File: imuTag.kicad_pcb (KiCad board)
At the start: 4 copper layers, 41.3 x 40 mm, 47 parts, among them J1 Conn_02x05_Odd_Even, J2 Conn_01x04_Pin, J3 Conn_01x02_Pin, Q1 DMG2305UX-13, U1 E73-2G4M08S1C, U2 ME6211C30M5G-N, U3 GD25Q64ESIG, U4 LSM6DSV16XTR, U5 LIS2MDLTR, Y2 Crystal

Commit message: Update PCB layout
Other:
- board text added: "GPIO"
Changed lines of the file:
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@@
 			(at 0 -2.38 90)
 			(layer "F.SilkS")
+			(hide yes)
 			(effects
 				(font
@@
 			(at 0 -1.43 270)
 			(layer "F.SilkS")
+			(hide yes)
 			(effects
 				(font
@@
 	)
 	(gr_text "FLASH"
-		(at 174.2694 116.3066 0)
+		(at 175.8188 116.3574 0)
 		(layer "F.SilkS")
 		(effects
@@
 	)
 	(gr_text "Magn."
-		(at 165.9382 117.0432 0)
+		(at 165.5064 114.9096 90)
 		(layer "F.SilkS")
 		(effects
@@
 		)
 	)
+	(gr_text "GPIO"
+		(at 164.3634 118.7196 90)
+		(layer "F.SilkS")
+		(effects
+			(font
+				(size 1 1)
+				(thickness 0.1)
+			)
+			(justify left bottom)
+		)
+	)
 	(gr_text "BTN1"
 		(at 155.9052 107.3404 305)
@@
 	)
 	(segment
-		(start 162.0126 114.7656)
-		(end 162.797 114.7656)
-		(width 0.4)
-		(layer "F.Cu")
-		(net 1)
-	)
-	(segment
 		(start 185.200083 107.773099)
 		(end 185.110822 107.86236)
@@
 	)
 	(segment
+		(start 162.797 114.7656)
+		(end 162.0126 114.7656)
+		(width 0.4)
+		(layer "F.Cu")
+		(net 1)
+	)
+	(segment
 		(start 156.880857 110.830657)
 		(end 157.607 111.5568)
@@
 	)
 	(segment
-		(start 162.797 114.7656)
-		(end 163.3982 115.3668)
-		(width 0.4)
-		(layer "F.Cu")
-		(net 1)
-	)
-	(segment
 		(start 163.824354 93.442046)
 		(end 164.15 93.1164)
@@
 	)
 	(segment
+		(start 163.385825 114.490175)
+		(end 163.072425 114.490175)
+		(width 0.4)
+		(layer "F.Cu")
+		(net 1)
+	)
+	(segment
 		(start 174.953 103.6331)
 		(end 175.1827 103.6331)
@@
 	)
 	(segment
+		(start 163.072425 114.490175)
+		(end 162.797 114.7656)
+		(width 0.4)
+		(layer "F.Cu")
+		(net 1)
+	)
+	(segment
 		(start 165.344 99.2786)
 		(end 167.249 101.1836)
@@
 	)
 	(via
-		(at 163.3982 115.3668)
+		(at 163.385825 114.490175)
 		(size 0.6)
 		(drill 0.4)

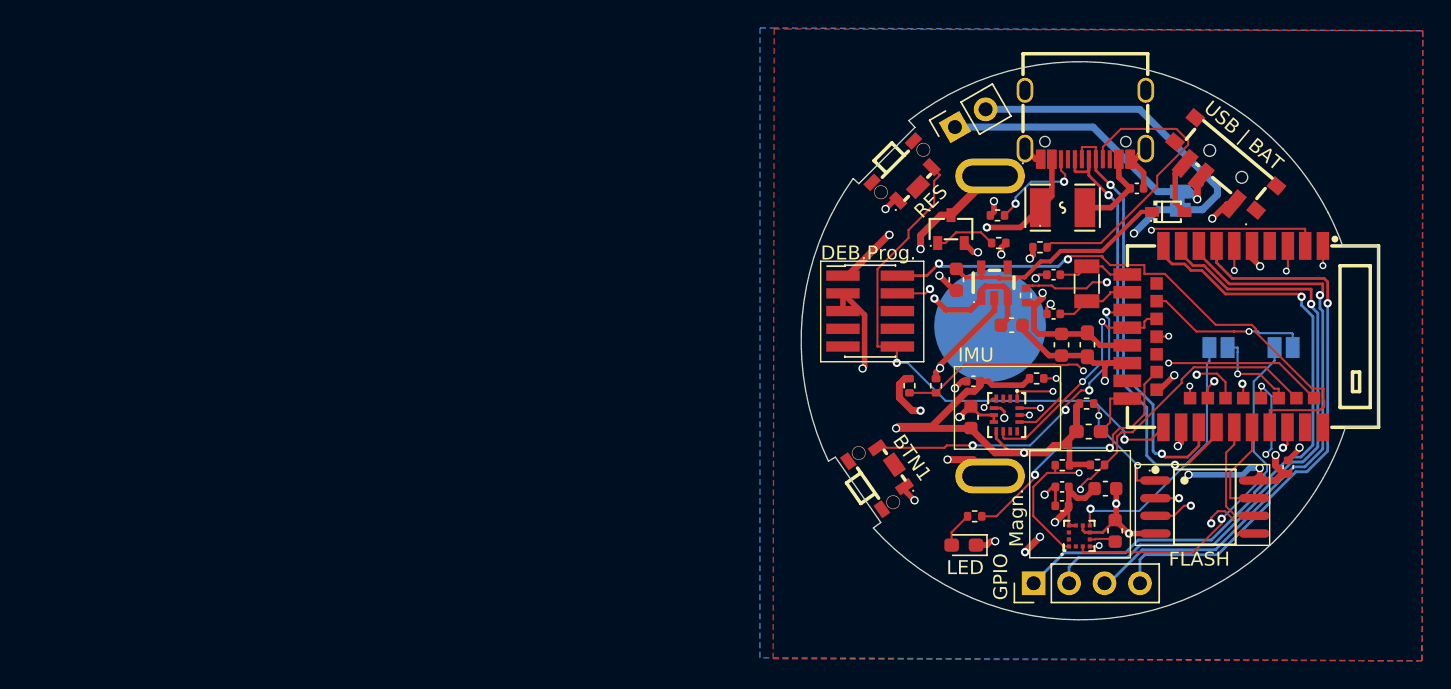
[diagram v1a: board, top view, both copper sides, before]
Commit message: feat: imuTag mini PCBA v1.0 – initial release
PCB layout, schematics (imuTag + sensors), custom EasyEDA symbol/footprint libraries with 3D models, design rules, and production outputs (BOM, placement, netlist).
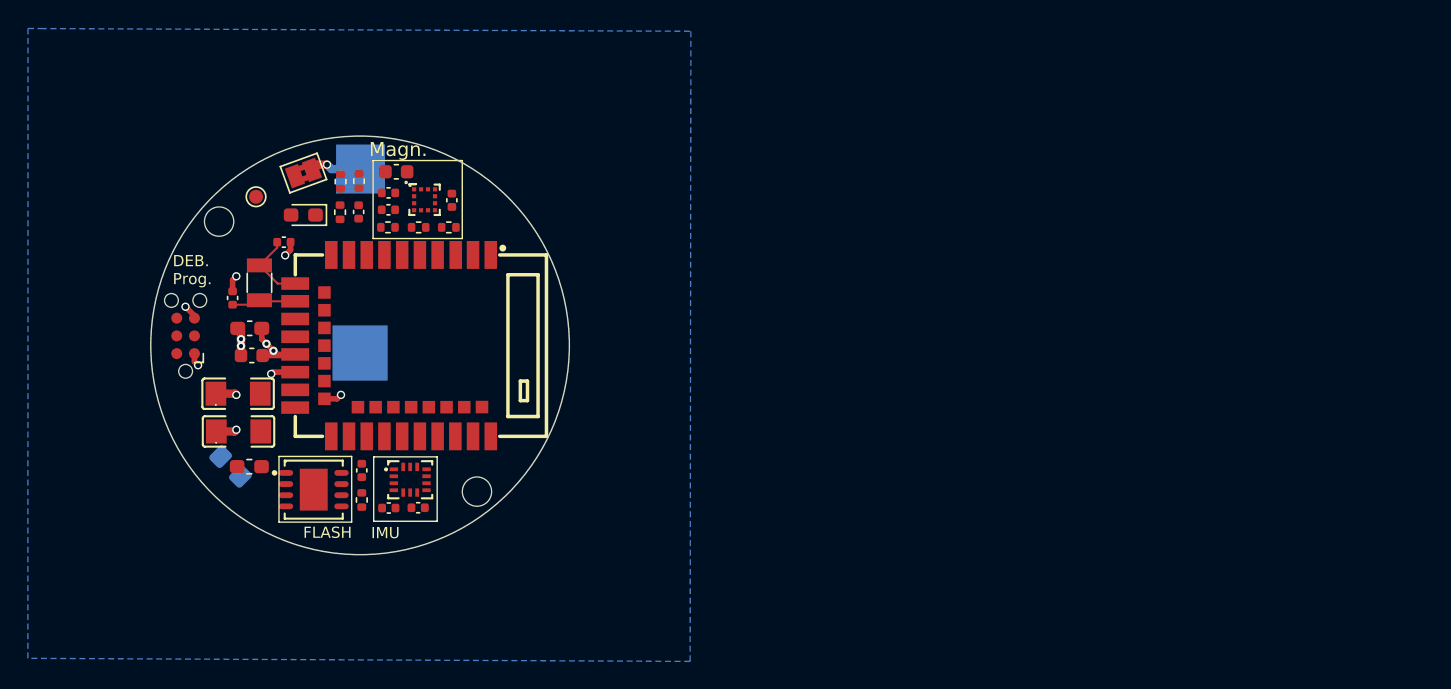
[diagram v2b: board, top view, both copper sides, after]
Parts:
- removed BAT1: BS-CR2032-8, EasyEDA:BAT-TH_MY-2032-22
- removed BTN1, RESET1: SW_Push, EasyEDA:SW-SMD_TS-1086EV-AR03526
- removed C3: 1u, Capacitor_SMD:C_0603_1608Metric
- removed D3: 1N5819WS, EasyEDA:SOD-323_L1.8-W1.3-LS2.5-RD
- removed F1: 1210L110/16WR, EasyEDA:F1210
- removed J2: Conn_01x04_Pin, Connector_PinHeader_2.54mm:PinHeader_1x04_P2.54mm_Vertical
- removed J3: Conn_01x02_Pin, Connector_PinSocket_2.54mm:PinSocket_1x02_P2.54mm_Vertical
- removed JP1, JP7: SolderJumper_2_Open, Jumper:SolderJumper-2_P1.3mm_Open_Pad1.0x1.5mm
- removed Q1: DMG2305UX-13, EasyEDA:SOT-23-3_L2.9-W1.3-P1.90-LS2.4-BR
- removed R10: 10K, Resistor_SMD:R_0402_1005Metric
- removed R4: 5K1, Resistor_SMD:R_0402_1005Metric
- removed R6: 100K, Resistor_SMD:R_0402_1005Metric
- removed U3: GD25Q64ESIG, EasyEDA:SOP-8_L5.3-W5.3-P1.27-LS8.0-BL
- removed USBC1: TYPE-C-31-M-12, EasyEDA:USB-C_SMD-TYPE-C-31-M-12_1
- removed VCCSEL1: MK-12C02-G015, EasyEDA:SW-SMD_G-SWITCH_MK-12C02-G015
- added BT1: Battery_Cell, EasyEDA:CR2032_Custom_Contacts_SMD_AirTagStyle, B.Cu at (122.4, 94.0)
- added C8: CL31A107MQHNNNE, EasyEDA:C1206, F.Cu at (109.2, 106.6)
- added H1: MountingHole, MountingHole:MountingHole_2.1mm, F.Cu at (126.2, 110.9)
- added H2: MountingHole, EasyEDA:Slot_1.2x3.0mm_NPTH, F.Cu at (129.1, 92.9)
- added H3: MountingHole, MountingHole:MountingHole_2.1mm, F.Cu at (107.8, 91.6)
- added TP1: TestPoint, TestPoint:TestPoint_Pad_D1.0mm, F.Cu at (110.4, 89.8)
- C1: value 0.1u -> 10n
- C16: value 0.22u -> 220n; footprint Capacitor_SMD:C_0603_1608Metric -> Capacitor_SMD:C_0402_1005Metric
- C18: footprint Capacitor_SMD:C_0603_1608Metric -> Capacitor_SMD:C_0402_1005Metric
- C2: value 1u -> CL31A107MQHNNNE; footprint Capacitor_SMD:C_0603_1608Metric -> EasyEDA:C1206
- C21: value 1u -> 10u
- J1: value Conn_02x05_Odd_Even -> Conn_ARM_SWD_TagConnect_TC2030-NL; footprint Connector_PinHeader_1.27mm:PinHeader_2x05_P1.27mm_Vertical_SMD -> Connector:Tag-Connect_TC2030-IDC-NL_2x03_P1.27mm_Vertical
- JP2: footprint Jumper:SolderJumper-2_P1.3mm_Bridged_Pad1.0x1.5mm -> Jumper:SolderJumper-2_P1.3mm_Bridged2Bar_Pad1.0x1.5mm; moved to F.Cu
- R1: value 5K1 -> 0R; footprint Resistor_SMD:R_0402_1005Metric -> Resistor_SMD:R_0805_2012Metric_Pad1.20x1.40mm_HandSolder; moved to B.Cu
- R11: value 10K -> 47K
- R16, R18: value 4K7 -> 47K
- U2: value ME6211C30M5G-N -> MX25R6435FZAIL0; footprint EasyEDA:SOT-23-5_L2.9-W1.6-P0.95-LS2.8-BL -> EasyEDA:WSON-8_L4.0-W4.0-P0.80-BL-EP-1
- moved C14 66.4 mm to (118.0, 109.4)
- moved JP2 62.9 mm to (113.8, 88.1), turned to -160 degrees
- moved L1 60.2 mm to (109.9, 109.1)
- moved C4 60.0 mm to (110.0, 99.2), turned to 180 degrees
- moved U1 59.6 mm to (120.2, 100.5)
- moved Y2 59.3 mm to (110.7, 96.0)
- moved C6 58.8 mm to (108.7, 97.1), turned to 90 degrees
- moved C5 58.0 mm to (110.1, 101.2), turned to 180 degrees
- moved R1 57.8 mm to (108.6, 109.1), turned to -45 degrees
- moved C1 55.8 mm to (117.8, 90.9), turned to 90 degrees
- moved C21 55.7 mm to (120.5, 88.0), turned to 0 degrees
- moved C2 55.7 mm to (109.1, 103.9), turned to 0 degrees
- moved C7 55.2 mm to (112.4, 93.1), turned to 0 degrees
- moved C16 53.1 mm to (124.4, 90.1)
- moved D2 52.9 mm to (113.8, 91.1)
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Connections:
- C1 pad 1: /+5V_USB_prot -> GND
- C1 pad 2: GND -> /BATTERY_PIN
- C2 pad 2: /+5V_USB -> /VBAT
- J1 pad 3: GND -> /RESET
- JP2 pad 1: VCC -> /VBAT
- JP2 pad 2: /VCC_1 -> VCC
- R1 pad 1: Net-(USBC1-CC2) -> VCC
- R1 pad 2: GND -> /RESET
- R2 pad 1: /VBAT -> VCC
- R3 pad 2: GND -> /GPIO_BAT_MEAS
- U1 pad 10: /AI3 -> unconnected-(U1-AI6-Pad10)
- U1 pad 14: /LIS2MDL_CS -> unconnected-(U1-P0.06-Pad14)
- U1 pad 15: /BTN1 -> unconnected-(U1-AI3-Pad15)
- U1 pad 20: unconnected-(U1-P12-Pad20) -> /LED1
- U1 pad 22: /LED1 -> unconnected-(U1-P0.07-Pad22)
- U1 pad 27: VCC -> unconnected-(U1-VBS-Pad27)
- U1 pad 29: /USB_D- -> unconnected-(U1-D--Pad29)
- U1 pad 31: /USB_D+ -> unconnected-(U1-D+-Pad31)
- U1 pad 38: /LIS2MDL_INT -> /GPIO_BAT_MEAS
- U1 pad 7: /AI0 -> unconnected-(U1-AI0-Pad7)
- U1 pad 8: /AI1 -> unconnected-(U1-AI5-Pad8)
- U1 pad 9: /AI2 -> unconnected-(U1-AI7-Pad9)
- U2 pad 1: /+5V_USB -> /QSPI_CS
- U2 pad 2: GND -> /QSPI_IO1
- U2 pad 3: /+5V_USB -> /QSPI_IO2
- U2 pad 4: unconnected-(U2-NC-Pad4) -> GND
- U2 pad 5: Net-(D3-K) -> /QSPI_IO0
- U5 pad 7: Net-(JP1-B) -> unconnected-(U5-INT/DRDY/SDO-Pad7)
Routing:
- net VCC: track 178.5 -> 6.92 mm, vias 13 -> 3
- net Net-(U5-CS): track 53.5 -> 0.00 mm, vias 2 -> 0
- net GND: track 62.6 -> 11.5 mm, vias 20 -> 9
- net /AI3: track 47.2 -> 0.00 mm, vias 1 -> 0
- net /AI2: track 45.2 -> 0.00 mm, vias 1 -> 0
- net /SWDCLK: track 43.7 -> 0.00 mm, vias 2 -> 0
- net /SWDIO: track 42.3 -> 0.00 mm, vias 2 -> 0
- net /AI1: track 42.1 -> 0.00 mm, vias 1 -> 0
- net /LSM6DSV16_INT1: track 40.9 -> 0.00 mm, vias 3 -> 0
- net /AI0: track 40.4 -> 0.00 mm, vias 1 -> 0
- net /RESET: track 39.7 -> 0.00 mm, vias 2 -> 0
- net /USB_D+: track 33.0 -> 0.00 mm, vias 2 -> 0
- net /SPI1_SCLK: track 32.0 -> 0.00 mm, vias 2 -> 0
- net /USB_D-: track 31.9 -> 0.00 mm, vias 2 -> 0
- net /I2C0_SCL: track 31.8 -> 0.00 mm, vias 2 -> 0
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- added copper zone on In2.Cu, net VCC
- removed copper zone on F.Cu, net GND
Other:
- board size 41.3 x 40 mm -> 30 x 30 mm
- board text added: "DEB. Prog."
- board text removed: "BTN1"
- board text removed: "Cut for current measurement"
- board text removed: "DEB.Prog."
- board text removed: "GPIO"
- board text removed: "LED"
- board text removed: "LIS2MDL SPI Option"
- board text removed: "RES"
- board text removed: "USB | BAT"

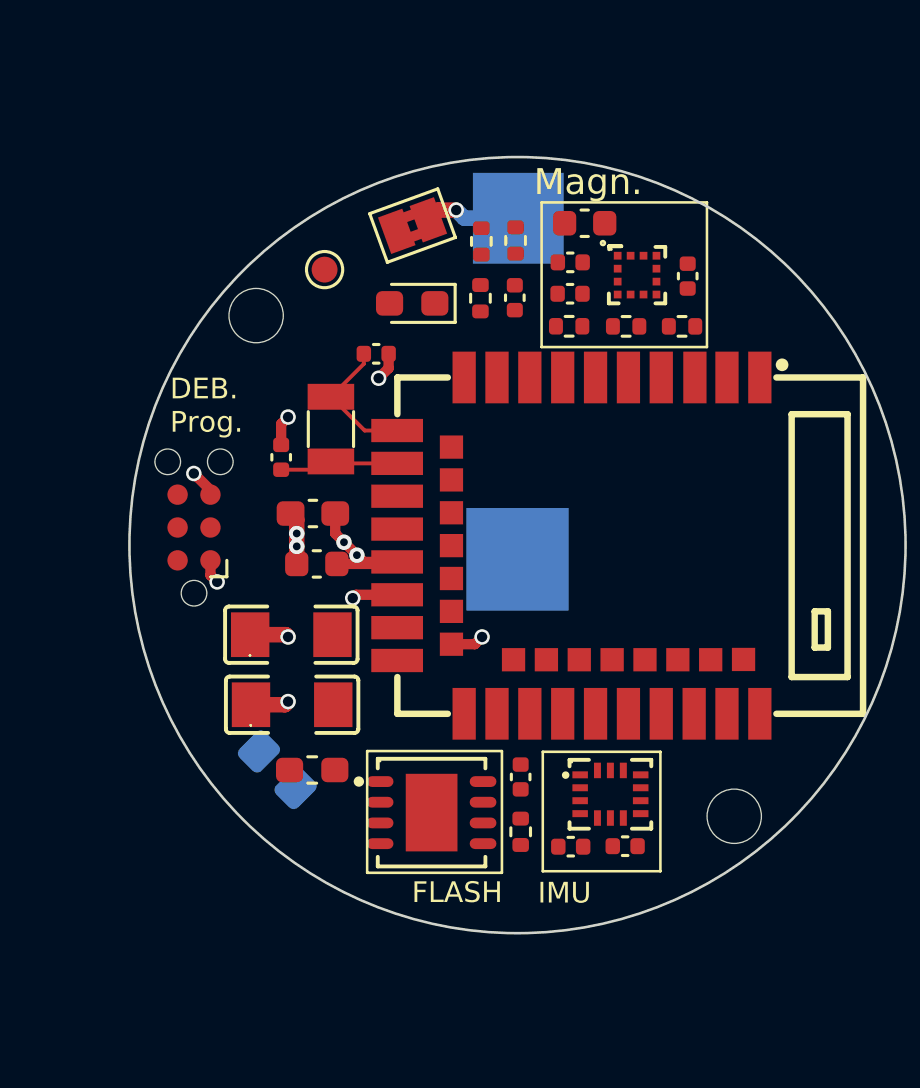
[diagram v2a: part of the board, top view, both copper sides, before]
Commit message: feat: import Spectra auto-route session into PCB layout
Applied Freerouting/Spectra session to imuTag.kicad_pcb, updating copper traces from the auto-router result.
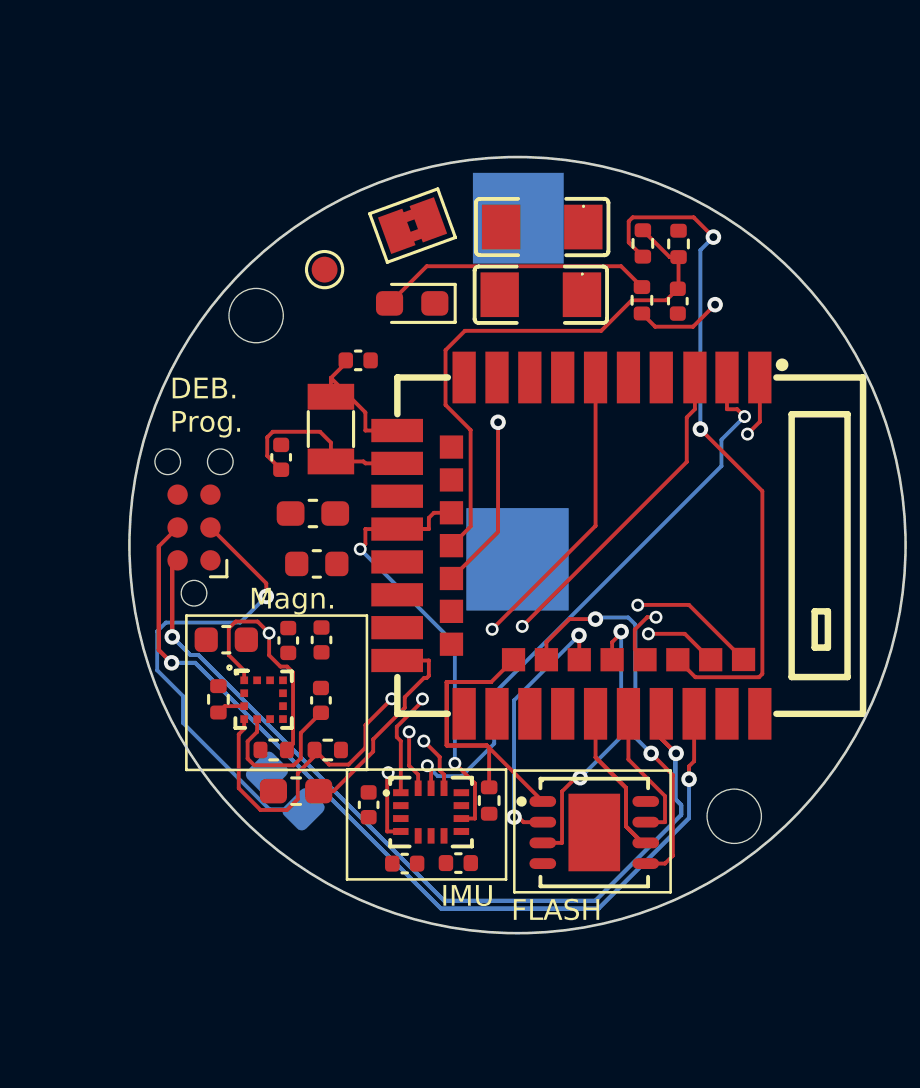
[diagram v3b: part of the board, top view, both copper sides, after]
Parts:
- moved U5 21.9 mm to (108.1, 106.4)
- moved C16 21.7 mm to (110.3, 106.5)
- moved R18 21.3 mm to (110.5, 108.4)
- moved R16 21.3 mm to (108.4, 108.4)
- moved C21 21.2 mm to (106.6, 104.1)
- moved R15 19.8 mm to (106.3, 106.4), turned to -90 degrees
- moved C8 18.5 mm to (118.8, 90.8), turned to 180 degrees
- moved C2 18.5 mm to (118.8, 88.2), turned to 180 degrees
- moved C19 18.2 mm to (109.0, 104.1), turned to -90 degrees
- moved C17 16.5 mm to (110.3, 104.1), turned to -90 degrees
- moved U4 6.97 mm to (114.5, 110.8)
- moved C20 6.48 mm to (115.6, 112.7)
- moved C18 6.45 mm to (113.5, 112.8)
- moved U2 6.34 mm to (120.8, 111.6)
- moved C1 6.30 mm to (124.1, 91.0)
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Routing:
- net /SWDCLK: track 0.00 -> 65.8 mm, vias 0 -> 2
- net /SWDIO: track 0.00 -> 64.8 mm, vias 0 -> 2
- net /SPI1_MOSI: track 0.00 -> 34.7 mm, vias 0 -> 2
- net /I2C0_SCL: track 0.00 -> 28.9 mm, vias 0 -> 2
- net /I2C0_SDA: track 0.00 -> 27.4 mm, vias 0 -> 2
- net /GPIO_BAT_MEAS: track 0.00 -> 26.9 mm, vias 0 -> 2
- net /SPI1_SCLK: track 0.00 -> 22.9 mm, vias 0 -> 2
- net /BATTERY_PIN: track 0.00 -> 21.3 mm
- net /LSM6DSV16_CS: track 0.00 -> 20.5 mm, vias 0 -> 2
- net /LED1: track 0.00 -> 20.4 mm, vias 0 -> 2
- net /SPI1_MISO: track 0.00 -> 19.3 mm, vias 0 -> 2
- net /LSM6DSV16_INT1: track 0.00 -> 18.8 mm, vias 0 -> 2
- net /RESET: track 0.00 -> 18.3 mm, vias 0 -> 1
- net /QSPI_CS: track 0.00 -> 17.5 mm
- net /LSM6DSV16_INT2: track 0.00 -> 17.5 mm, vias 0 -> 2
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
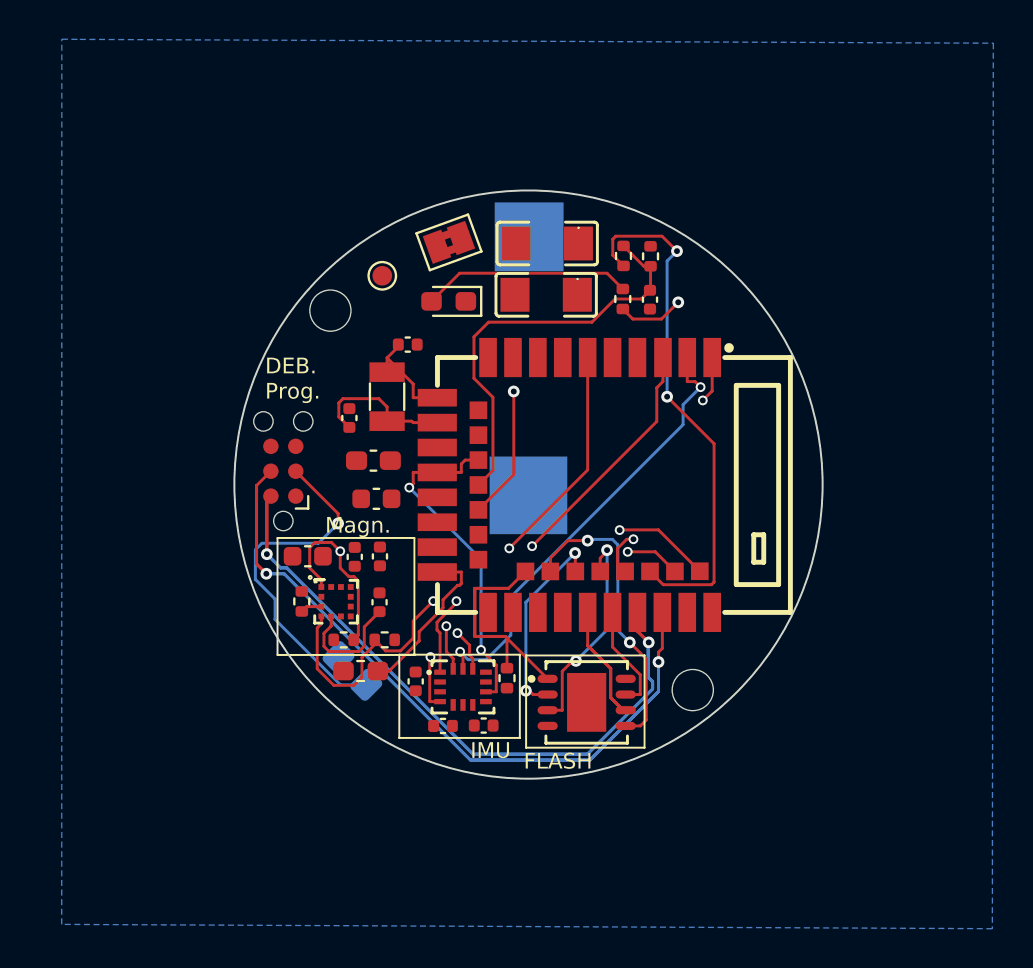
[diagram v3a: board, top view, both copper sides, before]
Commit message: feat: finalize schematic wiring
Completed all net connections across imuTag and sensors schematics. Design is electrically complete and ready for layout review.
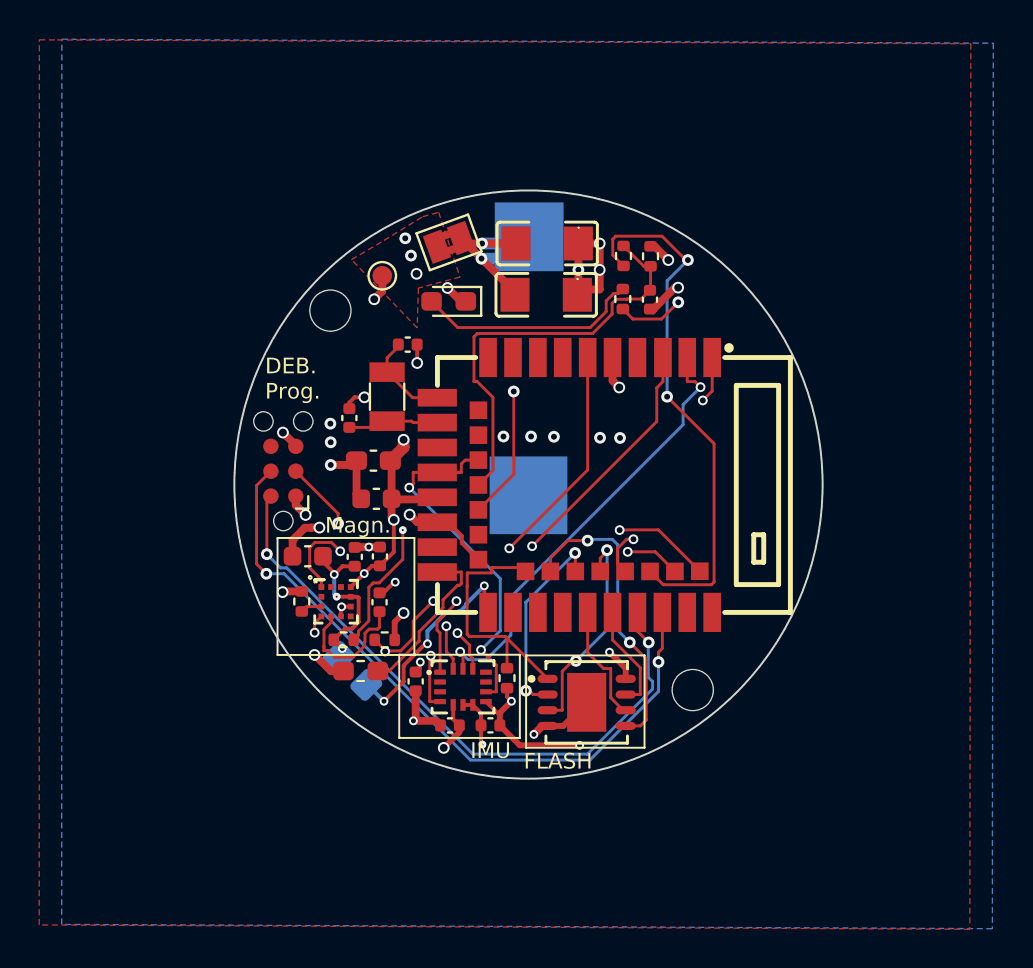
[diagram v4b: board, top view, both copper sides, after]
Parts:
- moved C18 2.42 mm to (115.9, 112.7)
- moved C20 1.72 mm to (113.9, 112.7), turned to 180 degrees
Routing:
- net VCC: track 0.00 -> 45.7 mm, vias 0 -> 19
- net GND: track 0.00 -> 39.6 mm, vias 0 -> 26
- net /SWDIO: track 64.8 -> 33.5 mm
- net /SWDCLK: track 65.8 -> 35.2 mm
- net /VBAT: track 0.00 -> 14.3 mm, vias 0 -> 2
- net /RESET: track 18.3 -> 26.5 mm, vias 1 -> 4
- net /QSPI_CS: track 17.5 -> 13.2 mm
- net /QSPI_CLK: track 10.0 -> 6.08 mm
- net Net-(U1-XL2): track 7.52 -> 4.65 mm
- net /I2C0_SDA: track 27.4 -> 24.9 mm, vias 2 -> 4
- net /I2C0_SCL: track 28.9 -> 30.6 mm, vias 2 -> 3
- net /LSM6DSV16_INT2: track 17.5 -> 18.3 mm
- net Net-(D2-A): track 10.7 -> 11.4 mm
- net Net-(U1-XL1): track 5.45 -> 4.74 mm
- net Net-(U5-C1): track 6.04 -> 6.67 mm
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- added copper zone on In2.Cu, net /VBAT
- added copper zone on F.Cu, net GND
- added copper zone on F.Cu, net VCC
